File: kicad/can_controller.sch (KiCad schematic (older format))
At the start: 13 parts

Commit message: Add regulator library
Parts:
- added U?: AP63205WU-7, SOIC_05WU-7, symbol 2020-02-12_13-05-37:AP63205WU-7
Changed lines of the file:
@@
 	8100 1200 8250 1200
 Connection ~ 8250 1200
+$Comp
+L 2020-02-12_13-05-37:AP63205WU-7 U?
+U 1 1 5E440D38
+P 5300 1100
+F 0 "U?" H 6100 1487 60  0000 C CNN
+F 1 "AP63205WU-7" H 6100 1381 60  0000 C CNN
+F 2 "SOIC_05WU-7" H 6100 1340 60  0001 C CNN
+F 3 "" H 5300 1100 60  0000 C CNN
+	1    5300 1100
+	1    0    0    -1
+$EndComp
 $EndSCHEMATC

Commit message: Add power
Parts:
- removed H?: MountingHole_Pad, symbol Mechanical:MountingHole_Pad
- added BT?: Battery_Cell, symbol Device:Battery_Cell
- added C?: 10uF, symbol Device:C_Small
- added C?: 100nF, symbol Device:C_Small
- added C? (x2): 22uF, symbol Device:C_Small
- added C? (x7): 0.1uF, symbol Device:C_Small
- added L?: 4.7uH, symbol Device:L_Small
- added SW?: SW_Push_Dual, symbol Switch:SW_Push_Dual
- C? (x2): value C_Small -> 0.1uF
- C?: value C_Small -> 2.2uF
- C?: value C_Small -> 10uF
- D?: value D_Small -> NSR1020MW2
- D?: value D_Schottky_Small -> MBR120ESFT1G1
- L?: value L_Small -> 6.8uH
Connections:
- net labels added: 12V, CAN_HS_H, CAN_HS_L, CAN_MS_H, CAN_MS_L
- wire segments 45 -> 137
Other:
- moved on the sheet: C?

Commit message: Update kicad files
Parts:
- U?: symbol 2020-02-12_13-05-37:AP63205WU-7 -> can_controller-rescue:AP63205WU-7-2020-02-12_13-05-37
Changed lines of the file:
@@
 	8800 1200 8950 1200
 $Comp
-L 2020-02-12_13-05-37:AP63205WU-7 U?
+L can_controller-rescue:AP63205WU-7-2020-02-12_13-05-37 U?
 U 1 1 5E440D38
 P 1900 1200

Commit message: Add programming and sim headers
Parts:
- added J?: Header for SIM800L, symbol Connector:Conn_01x07_Female
- added J?: Programming conn, symbol Connector:Conn_01x04_Male
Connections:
- net +3V3: now also J?.4 (Pin_4), J?.5 (Pin_5)
- net +5V: now also J?.7 (Pin_7)
- net GND: now also J?.1 (Pin_1), J?.2 (Pin_2), J?.6 (Pin_6)
- net SWDIO: now reaches U?.46 (PA13)
- net SWDIO: now also J?.3 (Pin_3)
- net SWCLK: now reaches U?.49 (PA14)
- net SWCLK: now also J?.2 (Pin_2)
- net RX: now reaches U?.51 (PC10)
- net RX: now also J?.3 (Pin_3)
- net TX: now reaches U?.52 (PC11)
- net TX: now also J?.4 (Pin_4)
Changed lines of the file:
@@
 	6200 6050 6100 6050
 Connection ~ 6100 6050
+$Comp
+L Connector:Conn_01x07_Female J?
+U 1 1 5E461B75
+P 3250 4700
+F 0 "J?" H 3278 4726 50  0000 L CNN
+F 1 "Header for SIM800L" H 3278 4635 50  0000 L CNN
+F 2 "" H 3250 4700 50  0001 C CNN
+F 3 "~" H 3250 4700 50  0001 C CNN
+	1    3250 4700
+	-1   0    0    1
+$EndComp
+$Comp
+L power:GND #PWR?
+U 1 1 5E47C6F5
+P 3650 5200
+F 0 "#PWR?" H 3650 4950 50  0001 C CNN
+F 1 "GND" H 3655 5027 50  0000 C CNN
+F 2 "" H 3650 5200 50  0001 C CNN
+F 3 "" H 3650 5200 50  0001 C CNN
+	1    3650 5200
+	1    0    0    -1
+$EndComp
+Wire Wire Line
+	3450 4900 3650 4900
+Wire Wire Line
+	3650 4900 3650 5200
+$Comp
+L power:+5V #PWR?
+U 1 1 5E489670
+P 3750 4150
+F 0 "#PWR?" H 3750 4000 50  0001 C CNN
+F 1 "+5V" H 3765 4323 50  0000 C CNN
+F 2 "" H 3750 4150 50  0001 C CNN
+F 3 "" H 3750 4150 50  0001 C CNN
+	1    3750 4150
+	1    0    0    -1
+$EndComp
+$Comp
+L power:+3V3 #PWR?
+U 1 1 5E489DD7
+P 4050 4150
+F 0 "#PWR?" H 4050 4000 50  0001 C CNN
+F 1 "+3V3" H 4065 4323 50  0000 C CNN
+F 2 "" H 4050 4150 50  0001 C CNN
+F 3 "" H 4050 4150 50  0001 C CNN
+	1    4050 4150
+	1    0    0    -1
+$EndComp
+Wire Wire Line
+	3450 4400 3750 4400
+Wire Wire Line
+	3750 4400 3750 4150
+Wire Wire Line
+	3450 4500 3650 4500
+Wire Wire Line
+	3650 4500 3650 4900
+Connection ~ 3650 4900
+Wire Wire Line
+	3450 4600 4050 4600
+Wire Wire Line
+	4050 4600 4050 4150
+$Comp
+L Connector:Conn_01x04_Male J?
+U 1 1 5E4AB493
+P 7900 3750
+F 0 "J?" H 8008 4031 50  0000 C CNN
+F 1 "Programming conn" H 8008 3940 50  0000 C CNN
+F 2 "" H 7900 3750 50  0001 C CNN
+F 3 "~" H 7900 3750 50  0001 C CNN
+	1    7900 3750
+	-1   0    0    1
+$EndComp
+Wire Wire Line
+	7700 3650 7050 3650
+Wire Wire Line
+	7050 3650 7050 3550
+Wire Wire Line
+	7050 3550 6700 3550
+Wire Wire Line
+	6900 3750 6900 3650
+Wire Wire Line
+	6900 3650 6700 3650
+$Comp
+L power:+3V3 #PWR?
+U 1 1 5E4EC5D6
+P 7550 3550
+F 0 "#PWR?" H 7550 3400 50  0001 C CNN
+F 1 "+3V3" H 7565 3723 50  0000 C CNN
+F 2 "" H 7550 3550 50  0001 C CNN
+F 3 "" H 7550 3550 50  0001 C CNN
+	1    7550 3550
+	1    0    0    -1
+$EndComp
+Wire Wire Line
+	7700 3550 7550 3550
+$Comp
+L power:GND #PWR?
+U 1 1 5E4F3FB2
+P 7300 3900
+F 0 "#PWR?" H 7300 3650 50  0001 C CNN
+F 1 "GND" H 7305 3727 50  0000 C CNN
+F 2 "" H 7300 3900 50  0001 C CNN
+F 3 "" H 7300 3900 50  0001 C CNN
+	1    7300 3900
+	1    0    0    -1
+$EndComp
+Wire Wire Line
+	7700 3850 7300 3850
+Wire Wire Line
+	7300 3850 7300 3900
+Wire Wire Line
+	7700 3750 6900 3750
+Text Label 7400 3750 0    50   ~ 0
+SWCLK
+Text Label 7400 3650 0    50   ~ 0
+SWDIO
+Text Label 3500 4700 0    50   ~ 0
+TX
+Text Label 3500 4800 0    50   ~ 0
+RX
+Wire Wire Line
+	4800 4800 4800 4950
+Wire Wire Line
+	4800 4950 5300 4950
+Wire Wire Line
+	3450 4800 4800 4800
+Wire Wire Line
+	4750 4700 4750 5050
+Wire Wire Line
+	4750 5050 5300 5050
+Wire Wire Line
+	3450 4700 4750 4700
 $EndSCHEMATC

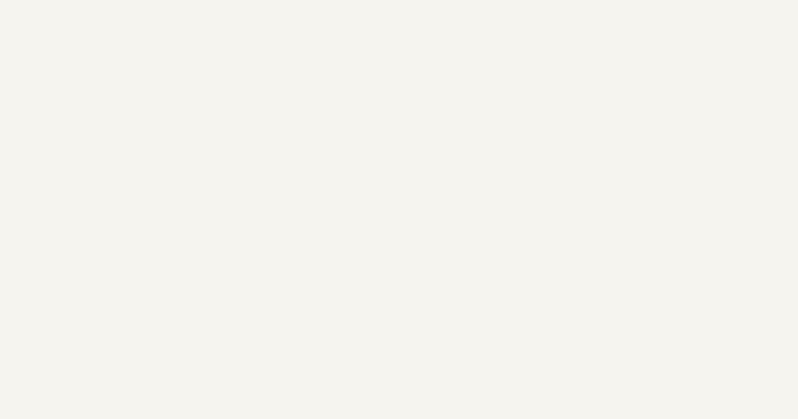
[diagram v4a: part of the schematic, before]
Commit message: Add 16 pin OBD2 socket wiring
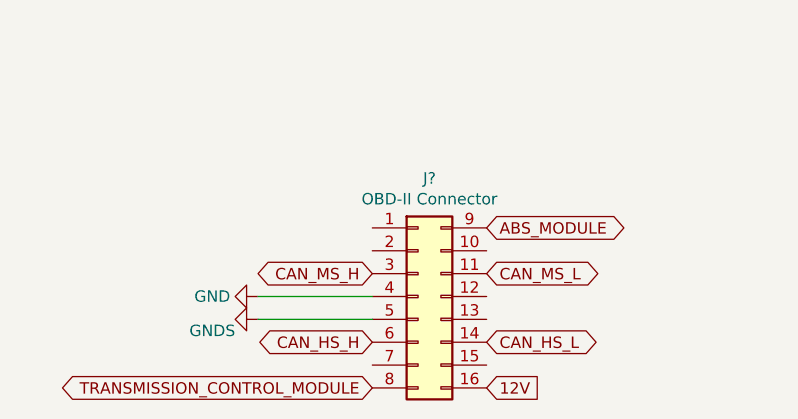
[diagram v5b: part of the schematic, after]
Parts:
- added J?: OBD-II Connector, symbol Connector_Generic:Conn_02x08_Top_Bottom
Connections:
- net 12V: now also J?.16 (Pin_16)
- net CAN_HS_H: now also J?.6 (Pin_6)
- net CAN_HS_L: now also J?.14 (Pin_14)
- net CAN_MS_H: now also J?.3 (Pin_3)
- net CAN_MS_L: now also J?.11 (Pin_11)
- net GND: now also J?.4 (Pin_4)
- new net ABS_MODULE: J?.9 (Pin_9)
- new net GNDS: J?.5 (Pin_5)
- new net TRANSMISSION_CONTROL_MODULE: J?.8 (Pin_8)
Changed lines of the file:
@@
 Wire Wire Line
 	3450 4700 4750 4700
+Text GLabel 1950 6950 0    50   BiDi ~ 0
+CAN_MS_H
+Text GLabel 2450 6950 2    50   BiDi ~ 0
+CAN_MS_L
+Text GLabel 1950 7250 0    50   BiDi ~ 0
+CAN_HS_H
+Text GLabel 2450 7250 2    50   BiDi ~ 0
+CAN_HS_L
+$Comp
+L power:GND #PWR?
+U 1 1 5E4CE02E
+P 1450 7050
+F 0 "#PWR?" H 1450 6800 50  0001 C CNN
+F 1 "GND" V 1450 6850 50  0000 C CNN
+F 2 "" H 1450 7050 50  0001 C CNN
+F 3 "" H 1450 7050 50  0001 C CNN
+	1    1450 7050
+	0    1    1    0
+$EndComp
+Text GLabel 2450 7450 2    50   Input ~ 0
+12V
+Wire Wire Line
+	1450 7050 1950 7050
+$Comp
+L Connector_Generic:Conn_02x08_Top_Bottom J?
+U 1 1 5E4885F7
+P 2150 7050
+F 0 "J?" H 2200 7567 50  0000 C CNN
+F 1 "OBD-II Connector" H 2200 7476 50  0000 C CNN
+F 2 "" H 2150 7050 50  0001 C CNN
+F 3 "~" H 2150 7050 50  0001 C CNN
+	1    2150 7050
+	1    0    0    -1
+$EndComp
+$Comp
+L power:GNDS #PWR?
+U 1 1 5E564AF3
+P 1450 7150
+F 0 "#PWR?" H 1450 6900 50  0001 C CNN
+F 1 "GNDS" V 1500 6950 50  0000 C CNN
+F 2 "" H 1450 7150 50  0001 C CNN
+F 3 "" H 1450 7150 50  0001 C CNN
+	1    1450 7150
+	0    1    1    0
+$EndComp
+Wire Wire Line
+	1450 7150 1950 7150
+Text GLabel 1950 7450 0    50   BiDi ~ 0
+TRANSMISSION_CONTROL_MODULE
+Text GLabel 2450 6750 2    50   BiDi ~ 0
+ABS_MODULE
 $EndSCHEMATC

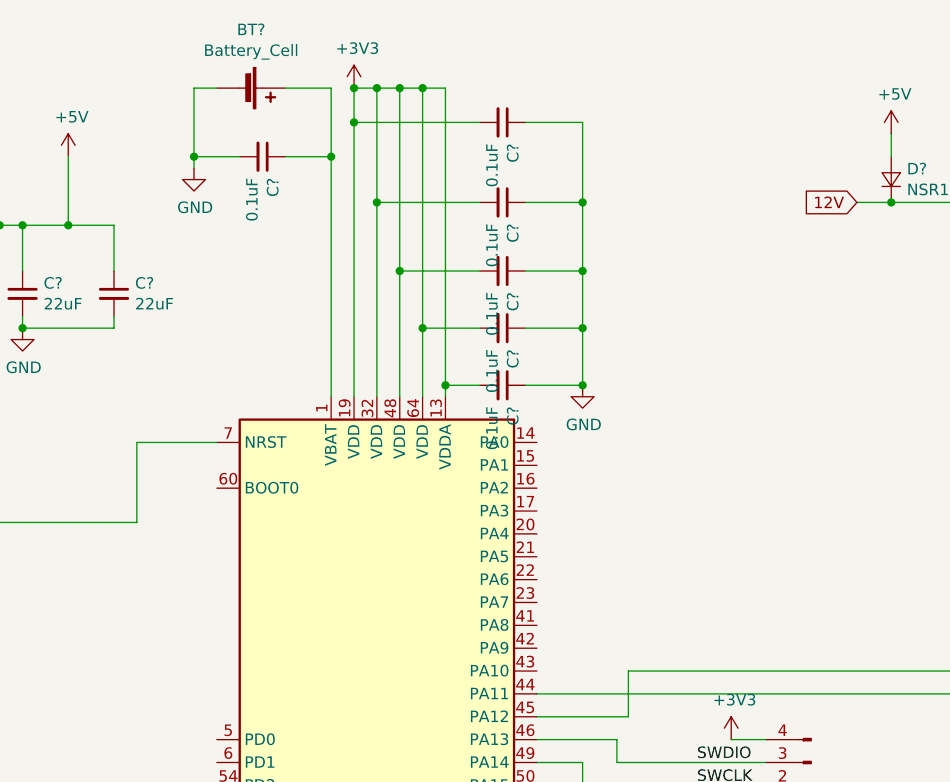
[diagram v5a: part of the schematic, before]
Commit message: Add power led
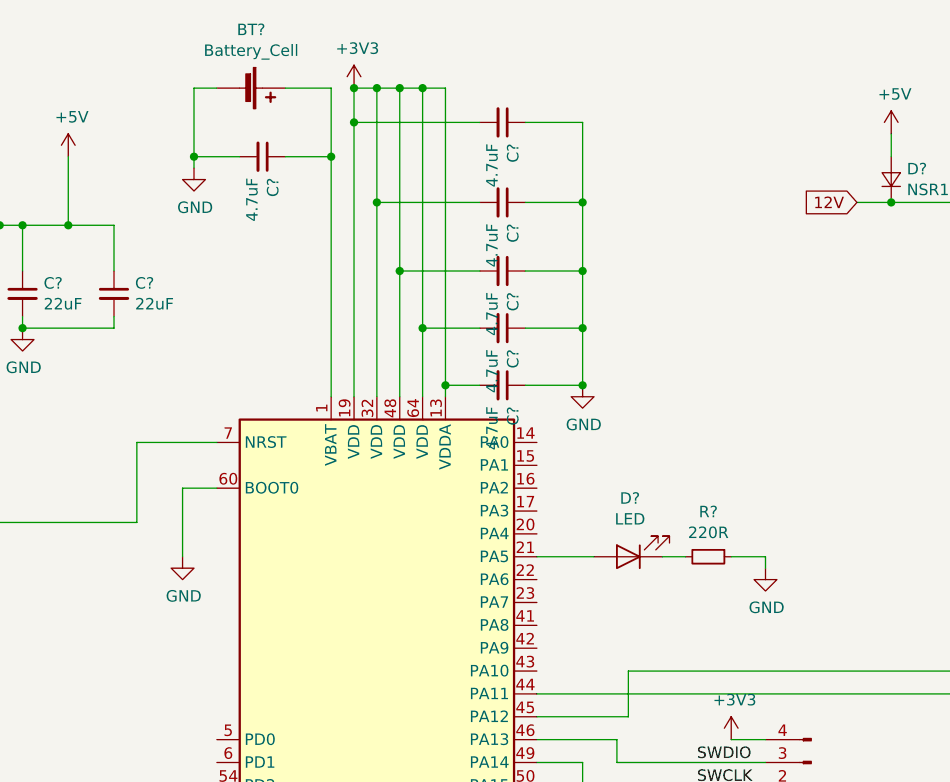
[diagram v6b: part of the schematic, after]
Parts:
- added D?: LED, symbol Device:LED
- added R?: 220R, symbol Device:R_Small
- C? (x6): value 0.1uF -> 4.7uF
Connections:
- net GND: now also U?.60 (BOOT0), R?.1
- net at U?.21 (PA5): now also D?.2 (A)
- new net: D?.1 (K), R?.2
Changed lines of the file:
@@
 P 6550 850
 F 0 "C?" H 6642 896 50  0000 L CNN
-F 1 "0.1uF" H 6642 805 50  0000 L CNN
+F 1 "4.7uF" H 6642 805 50  0000 L CNN
 F 2 "" H 6550 850 50  0001 C CNN
 F 3 "~" H 6550 850 50  0001 C CNN
@@
 P 6550 1200
 F 0 "C?" H 6642 1246 50  0000 L CNN
-F 1 "0.1uF" H 6642 1155 50  0000 L CNN
+F 1 "4.7uF" H 6642 1155 50  0000 L CNN
 F 2 "" H 6550 1200 50  0001 C CNN
 F 3 "~" H 6550 1200 50  0001 C CNN
@@
 P 6550 1500
 F 0 "C?" H 6642 1546 50  0000 L CNN
-F 1 "0.1uF" H 6642 1455 50  0000 L CNN
+F 1 "4.7uF" H 6642 1455 50  0000 L CNN
 F 2 "" H 6550 1500 50  0001 C CNN
 F 3 "~" H 6550 1500 50  0001 C CNN
@@
 P 6550 1750
 F 0 "C?" H 6642 1796 50  0000 L CNN
-F 1 "0.1uF" H 6642 1705 50  0000 L CNN
+F 1 "4.7uF" H 6642 1705 50  0000 L CNN
 F 2 "" H 6550 1750 50  0001 C CNN
 F 3 "~" H 6550 1750 50  0001 C CNN
@@
 P 6550 2000
 F 0 "C?" H 6642 2046 50  0000 L CNN
-F 1 "0.1uF" H 6642 1955 50  0000 L CNN
+F 1 "4.7uF" H 6642 1955 50  0000 L CNN
 F 2 "" H 6550 2000 50  0001 C CNN
 F 3 "~" H 6550 2000 50  0001 C CNN
@@
 P 5500 1000
 F 0 "C?" H 5592 1046 50  0000 L CNN
-F 1 "0.1uF" H 5592 955 50  0000 L CNN
+F 1 "4.7uF" H 5592 955 50  0000 L CNN
 F 2 "" H 5500 1000 50  0001 C CNN
 F 3 "~" H 5500 1000 50  0001 C CNN
@@
 Text GLabel 2450 6750 2    50   BiDi ~ 0
 ABS_MODULE
+$Comp
+L power:GND #PWR?
+U 1 1 5E52F399
+P 5150 2750
+F 0 "#PWR?" H 5150 2500 50  0001 C CNN
+F 1 "GND" H 5155 2577 50  0000 C CNN
+F 2 "" H 5150 2750 50  0001 C CNN
+F 3 "" H 5150 2750 50  0001 C CNN
+	1    5150 2750
+	1    0    0    -1
+$EndComp
+Wire Wire Line
+	5300 2450 5150 2450
+Wire Wire Line
+	5150 2450 5150 2750
+$Comp
+L Device:LED D?
+U 1 1 5E53A7DB
+P 7100 2750
+F 0 "D?" H 7093 2495 50  0000 C CNN
+F 1 "LED" H 7093 2586 50  0000 C CNN
+F 2 "" H 7100 2750 50  0001 C CNN
+F 3 "~" H 7100 2750 50  0001 C CNN
+	1    7100 2750
+	-1   0    0    1
+$EndComp
+$Comp
+L power:GND #PWR?
+U 1 1 5E53B550
+P 7700 2800
+F 0 "#PWR?" H 7700 2550 50  0001 C CNN
+F 1 "GND" H 7705 2627 50  0000 C CNN
+F 2 "" H 7700 2800 50  0001 C CNN
+F 3 "" H 7700 2800 50  0001 C CNN
+	1    7700 2800
+	1    0    0    -1
+$EndComp
+$Comp
+L Device:R_Small R?
+U 1 1 5E540995
+P 7450 2750
+F 0 "R?" V 7254 2750 50  0000 C CNN
+F 1 "220R" V 7345 2750 50  0000 C CNN
+F 2 "" H 7450 2750 50  0001 C CNN
+F 3 "~" H 7450 2750 50  0001 C CNN
+	1    7450 2750
+	0    1    1    0
+$EndComp
+Wire Wire Line
+	6700 2750 6950 2750
+Wire Wire Line
+	7250 2750 7350 2750
+Wire Wire Line
+	7550 2750 7700 2750
+Wire Wire Line
+	7700 2750 7700 2800
 $EndSCHEMATC

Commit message: Finalize schema
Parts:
- removed U?: AP63205WU-7, SOIC_05WU-7, symbol can_controller-rescue:AP63205WU-7-2020-02-12_13-05-37
- added C? (x2): 20pF, symbol Device:C_Small
- added D?: RGB_LED_HV, symbol can_controller-rescue:RGB_LED_HV
- added F?: Fuse, 0603, symbol Device:Fuse
- added JP? (x2): Jumper_NO_Small, symbol Device:Jumper_NO_Small
- added R?: 220R, symbol Device:R_Small
- added R? (x2): 120, symbol Device:R_Small
- added U?: AP63205WU-7-2020-02-12_13-05-37, SOIC_05WU-7, symbol can_controller-rescue:AP63205WU-7-2020-02-12_13-05-37
- added Y?: 8Mhz, symbol Device:Crystal_Small
- C?: value C_Small -> 0.1uF
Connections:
- net +5V: now also U?.1 (FB)
- net 12V: now also F?.1, U?.2 (EN), U?.3 (VIN); no longer J?.16 (Pin_16)
- net CAN_HS_H: now also JP?.1
- net CAN_HS_L: now also R?.2
- net CAN_MS_L: now also R?.2
- net GND: now also C?.2, C?.2, R?.1, U?.4 (GND)
- net at U?.23 (PA7): now also D?.2 (BA)
- net at U?.41 (PA8): now also D?.4 (GA)
- net at U?.42 (PA9): now also D?.1 (RA)
- net at U?.5 (PD0): now also C?.1, Y?.1
- net at U?.6 (PD1): now also C?.1, Y?.2
- net at C?.2, L?.1: now also U?.5 (SW)
- net at C?.1: now also U?.6 (BST)
- new net: F?.2, J?.16 (Pin_16)
- new net: D?.3 (K), R?.2
- new net: JP?.2, R?.1 (x2)
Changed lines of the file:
@@
 P 9950 4350
 F 0 "C?" V 9721 4350 50  0000 C CNN
-F 1 "C_Small" V 9812 4350 50  0000 C CNN
+F 1 "0.1uF" V 9812 4350 50  0000 C CNN
 F 2 "" H 9950 4350 50  0001 C CNN
 F 3 "~" H 9950 4350 50  0001 C CNN
@@
 Wire Wire Line
 	8800 1200 8950 1200
-$Comp
-L can_controller-rescue:AP63205WU-7-2020-02-12_13-05-37 U?
-U 1 1 5E440D38
-P 1900 1200
-F 0 "U?" H 2700 1587 60  0000 C CNN
-F 1 "AP63205WU-7" H 2700 1481 60  0000 C CNN
-F 2 "SOIC_05WU-7" H 2700 1440 60  0001 C CNN
-F 3 "" H 1900 1200 60  0000 C CNN
-	1    1900 1200
-	1    0    0    -1
-$EndComp
 $Comp
 L power:GND #PWR?
@@
 	4850 1300 4650 1300
 Connection ~ 4650 1300
-Text GLabel 10150 3350 2    50   BiDi ~ 0
+Text GLabel 10700 3350 2    50   BiDi ~ 0
 CAN_MS_H
-Text GLabel 10150 3450 2    50   BiDi ~ 0
+Text GLabel 10700 3450 2    50   BiDi ~ 0
 CAN_MS_L
-Text GLabel 10100 4700 2    50   BiDi ~ 0
+Text GLabel 10700 4700 2    50   BiDi ~ 0
 CAN_HS_H
-Text GLabel 10100 4800 2    50   BiDi ~ 0
+Text GLabel 10700 4800 2    50   BiDi ~ 0
 CAN_HS_L
-Wire Wire Line
-	10100 4800 9850 4800
-Wire Wire Line
-	10100 4700 9850 4700
-Wire Wire Line
-	10150 3450 9850 3450
-Wire Wire Line
-	10150 3350 9850 3350
 $Comp
 L power:GND #PWR?
@@
 Wire Wire Line
 	3450 4700 4750 4700
-Text GLabel 1950 6950 0    50   BiDi ~ 0
-CAN_MS_H
 Text GLabel 2450 6950 2    50   BiDi ~ 0
 CAN_MS_L
-Text GLabel 1950 7250 0    50   BiDi ~ 0
-CAN_HS_H
 Text GLabel 2450 7250 2    50   BiDi ~ 0
 CAN_HS_L
@@
 	0    1    1    0
 $EndComp
-Text GLabel 2450 7450 2    50   Input ~ 0
+Text GLabel 2750 7450 2    50   Input ~ 0
 12V
 Wire Wire Line
@@
 P 7700 2800
 F 0 "#PWR?" H 7700 2550 50  0001 C CNN
-F 1 "GND" H 7705 2627 50  0000 C CNN
+F 1 "GND" H 7600 2700 50  0000 C CNN
 F 2 "" H 7700 2800 50  0001 C CNN
 F 3 "" H 7700 2800 50  0001 C CNN
@@
 Wire Wire Line
 	7700 2750 7700 2800
+$Comp
+L Device:Crystal_Small Y?
+U 1 1 5E518EA3
+P 4850 3550
+F 0 "Y?" H 4850 3700 50  0000 C CNN
+F 1 "8Mhz" H 4850 3800 50  0000 C CNN
+F 2 "" H 4850 3550 50  0001 C CNN
+F 3 "~" H 4850 3550 50  0001 C CNN
+	1    4850 3550
+	-1   0    0    1
+$EndComp
+Wire Wire Line
+	5300 3650 4750 3650
+Wire Wire Line
+	4750 3650 4750 3550
+Wire Wire Line
+	4950 3500 4950 3550
+Wire Wire Line
+	4950 3550 5300 3550
+Connection ~ 4950 3550
+Connection ~ 4750 3550
+Wire Wire Line
+	4750 3550 4750 3500
+$Comp
+L Device:C_Small C?
+U 1 1 5E550D81
+P 4750 3400
+F 0 "C?" H 4842 3446 50  0000 L CNN
+F 1 "20pF" H 4842 3355 50  0000 L CNN
+F 2 "" H 4750 3400 50  0001 C CNN
+F 3 "~" H 4750 3400 50  0001 C CNN
+	1    4750 3400
+	-1   0    0    1
+$EndComp
+$Comp
+L Device:C_Small C?
+U 1 1 5E55120B
+P 4950 3400
+F 0 "C?" H 4800 3450 50  0000 L CNN
+F 1 "20pF" H 4700 3350 50  0000 L CNN
+F 2 "" H 4950 3400 50  0001 C CNN
+F 3 "~" H 4950 3400 50  0001 C CNN
+	1    4950 3400
+	-1   0    0    1
+$EndComp
+$Comp
+L power:GND #PWR?
+U 1 1 5E55588B
+P 4850 3200
+F 0 "#PWR?" H 4850 2950 50  0001 C CNN
+F 1 "GND" H 4855 3027 50  0000 C CNN
+F 2 "" H 4850 3200 50  0001 C CNN
+F 3 "" H 4850 3200 50  0001 C CNN
+	1    4850 3200
+	-1   0    0    1
+$EndComp
+Wire Wire Line
+	4750 3300 4750 3200
+Wire Wire Line
+	4750 3200 4850 3200
+Wire Wire Line
+	4850 3200 4950 3200
+Wire Wire Line
+	4950 3200 4950 3300
+Connection ~ 4850 3200
+$Comp
+L can_controller-rescue:RGB_LED_HV D?
+U 1 1 5E59F238
+P 8300 2850
+F 0 "D?" H 8300 2383 50  0000 C CNN
+F 1 "RGB_LED_HV" H 8300 2474 50  0000 C CNN
+F 2 "" H 8300 2800 50  0001 C CNN
+F 3 "~" H 8300 2800 50  0001 C CNN
+	1    8300 2850
+	-1   0    0    1
+$EndComp
+Wire Wire Line
+	6700 3150 8100 3150
+Wire Wire Line
+	8100 3150 8100 3050
+Wire Wire Line
+	8100 2850 8050 2850
+Wire Wire Line
+	8050 2850 8050 3050
+Wire Wire Line
+	8050 3050 6700 3050
+Wire Wire Line
+	8100 2650 7950 2650
+Wire Wire Line
+	7950 2650 7950 2950
+Wire Wire Line
+	7950 2950 6700 2950
+$Comp
+L power:GND #PWR?
+U 1 1 5E5D3098
+P 8700 2900
+F 0 "#PWR?" H 8700 2650 50  0001 C CNN
+F 1 "GND" H 8600 2800 50  0000 C CNN
+F 2 "" H 8700 2900 50  0001 C CNN
+F 3 "" H 8700 2900 50  0001 C CNN
+	1    8700 2900
+	1    0    0    -1
+$EndComp
+$Comp
+L Device:R_Small R?
+U 1 1 5E5D3560
+P 8600 2850
+F 0 "R?" V 8404 2850 50  0000 C CNN
+F 1 "220R" V 8495 2850 50  0000 C CNN
+F 2 "" H 8600 2850 50  0001 C CNN
+F 3 "~" H 8600 2850 50  0001 C CNN
+	1    8600 2850
+	0    1    1    0
+$EndComp
+Wire Wire Line
+	8700 2850 8700 2900
+$Comp
+L Device:Fuse F?
+U 1 1 5E5EB70D
+P 2600 7450
+F 0 "F?" V 2403 7450 50  0000 C CNN
+F 1 "Fuse" V 2494 7450 50  0000 C CNN
+F 2 "0603" V 2530 7450 50  0001 C CNN
+F 3 "~" H 2600 7450 50  0001 C CNN
+	1    2600 7450
+	0    1    1    0
+$EndComp
+Text GLabel 1950 7250 0    50   BiDi ~ 0
+CAN_HS_H
+Text GLabel 1950 6950 0    50   BiDi ~ 0
+CAN_MS_H
+Wire Wire Line
+	9850 3450 10450 3450
+Wire Wire Line
+	9850 4800 10500 4800
+Wire Wire Line
+	9850 4700 10300 4700
+$Comp
+L Device:Jumper_NO_Small JP?
+U 1 1 5E6A7EBF
+P 10400 4350
+F 0 "JP?" H 10400 4535 50  0000 C CNN
+F 1 "Jumper_NO_Small" H 10400 4444 50  0000 C CNN
+F 2 "" H 10400 4350 50  0001 C CNN
+F 3 "~" H 10400 4350 50  0001 C CNN
+	1    10400 4350
+	1    0    0    -1
+$EndComp
+$Comp
+L Device:R_Small R?
+U 1 1 5E6A8ADF
+P 10500 4500
+F 0 "R?" H 10559 4546 50  0000 L CNN
+F 1 "120" H 10559 4455 50  0000 L CNN
+F 2 "" H 10500 4500 50  0001 C CNN
+F 3 "~" H 10500 4500 50  0001 C CNN
+	1    10500 4500
+	1    0    0    -1
+$EndComp
+Wire Wire Line
+	10500 4350 10500 4400
+Wire Wire Line
+	10300 4350 10300 4700
+Connection ~ 10300 4700
+Wire Wire Line
+	10300 4700 10700 4700
+Wire Wire Line
+	10500 4600 10500 4800
+Connection ~ 10500 4800
+Wire Wire Line
+	10500 4800 10700 4800
+Wire Wire Line
+	9850 3350 10700 3350
+$Comp
+L Device:Jumper_NO_Small JP?
+U 1 1 5E6CD3C9
+P 10350 3000
+F 0 "JP?" H 10350 3185 50  0000 C CNN
+F 1 "Jumper_NO_Small" H 10450 3100 50  0000 C CNN
+F 2 "" H 10350 3000 50  0001 C CNN
+F 3 "~" H 10350 3000 50  0001 C CNN
+	1    10350 3000
+	1    0    0    -1
+$EndComp
+$Comp
+L Device:R_Small R?
+U 1 1 5E6CD3CF
+P 10450 3150
+F 0 "R?" H 10509 3196 50  0000 L CNN
+F 1 "120" H 10509 3105 50  0000 L CNN
+F 2 "" H 10450 3150 50  0001 C CNN
+F 3 "~" H 10450 3150 50  0001 C CNN
+	1    10450 3150
+	1    0    0    -1
+$EndComp
+Wire Wire Line
+	10450 3000 10450 3050
+Wire Wire Line
+	10250 3000 10250 3350
+Wire Wire Line
+	10450 3250 10450 3450
+Connection ~ 10450 3450
+Wire Wire Line
+	10450 3450 10700 3450
+$Comp
+L can_controller-rescue:AP63205WU-7-2020-02-12_13-05-37 U?
+U 1 1 5E6F7B55
+P 1900 1200
+F 0 "U?" H 2700 1587 60  0000 C CNN
+F 1 "AP63205WU-7-2020-02-12_13-05-37" H 2700 1481 60  0000 C CNN
+F 2 "SOIC_05WU-7" H 2700 1440 60  0001 C CNN
+F 3 "" H 1900 1200 60  0000 C CNN
+	1    1900 1200
+	1    0    0    -1
+$EndComp
 $EndSCHEMATC

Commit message: Jotain on tehty ehkä
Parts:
- removed D?: NSR1020MW2, symbol Device:D_Small
- gave numbers to parts that had none: 41
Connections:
- net CAN_MS_H: now also JP1.1
- net at U2.53 (PC12): now also J2.1 (Pin_1)
- no-connect marks 0 -> 45
